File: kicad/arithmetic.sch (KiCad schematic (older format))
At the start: 73 parts, among them J1 Conn_01x03_Male, J2 Conn_01x05_Male, J3 Conn_01x05_Male, J4 Conn_Coaxial, J5 Conn_Coaxial, J6 Conn_Coaxial, U1 LM317, U2 LM337, U3 OPA197xD, U4 OPA197xD, U5 OPA197xD

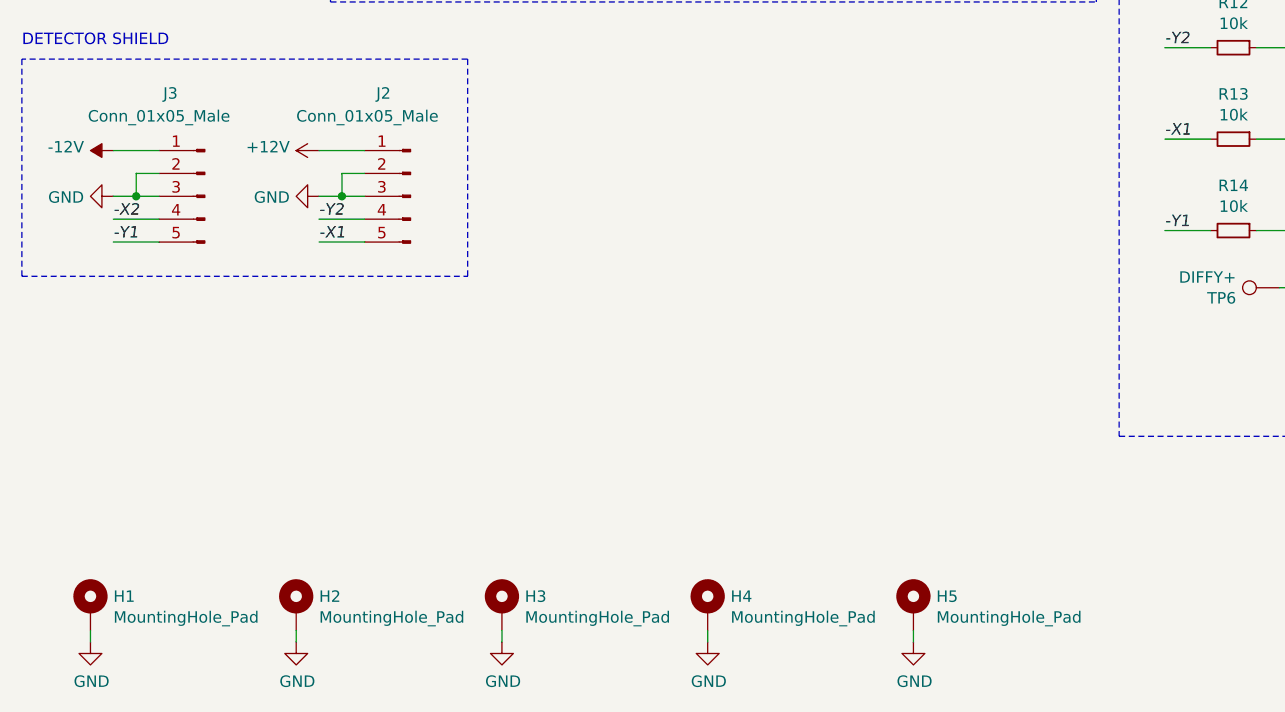
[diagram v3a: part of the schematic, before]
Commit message: adjusted arithmetic pcb for updated detector pcb
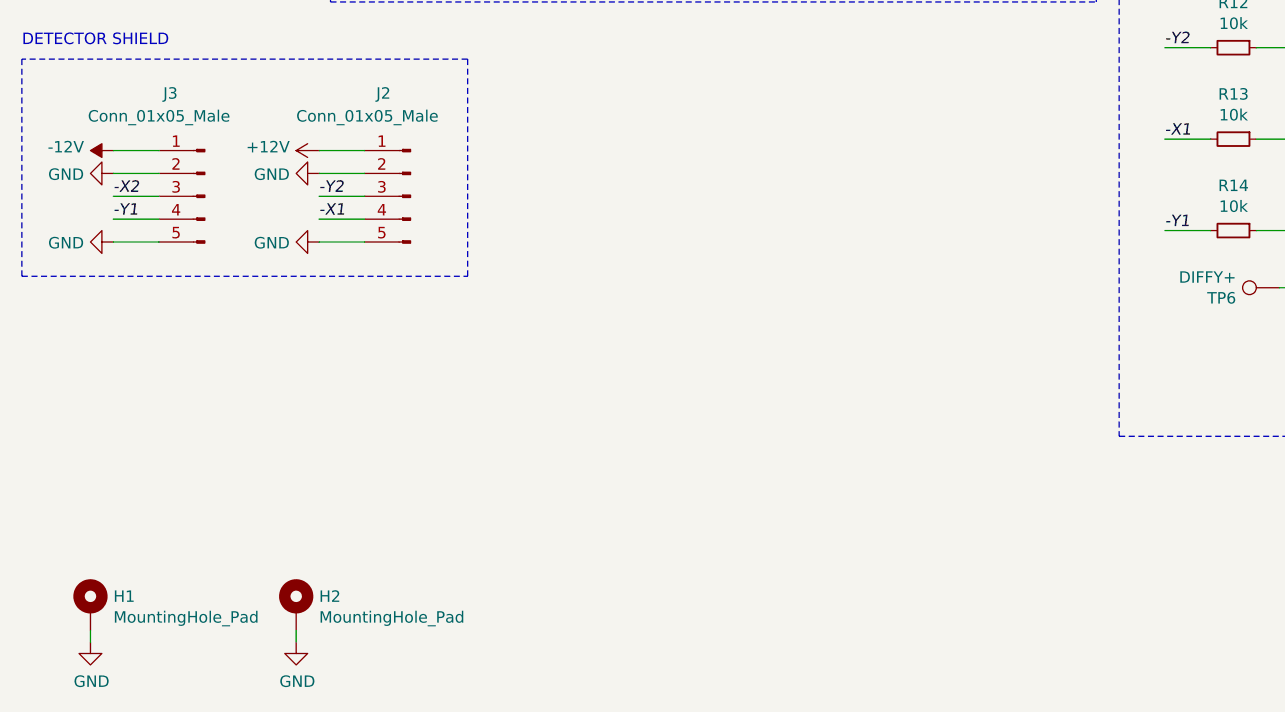
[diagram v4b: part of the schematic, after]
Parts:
- removed H3, H4, H5: MountingHole_Pad, MountingHole:MountingHole_2.7mm_M2.5_Pad, symbol Mechanical:MountingHole_Pad
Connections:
- net -X1: now also J2.4 (Pin_4); no longer J2.5 (Pin_5)
- net -X2: now also J3.3 (Pin_3); no longer J3.4 (Pin_4)
- net -Y1: now also J3.4 (Pin_4); no longer J3.5 (Pin_5)
- net -Y2: now also J2.3 (Pin_3); no longer J2.4 (Pin_4)
- net GND: now also J2.5 (Pin_5), J3.5 (Pin_5); no longer J2.3 (Pin_3), J3.3 (Pin_3)
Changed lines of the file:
@@
 Wire Notes Line
 	5300 750  1950 750
-Text Label 1900 5550 0    50   Italic 0
+Text Label 1900 5450 0    50   Italic 0
 -X1
+Text Label 1000 5350 0    50   Italic 0
+-X2
 Text Label 1000 5450 0    50   Italic 0
--X2
-Text Label 1000 5550 0    50   Italic 0
 -Y1
-Text Label 1900 5450 0    50   Italic 0
+Text Label 1900 5350 0    50   Italic 0
 -Y2
 Wire Wire Line
 	1000 5150 1200 5150
-Wire Wire Line
-	1200 5250 1100 5250
-Wire Wire Line
-	1000 5350 1100 5350
 Wire Wire Line
 	1200 5450 1000 5450
@@
 L power:GND #PWR02
 U 1 1 5EC11469
-P 1900 5350
+P 1900 5250
 AR Path="/5EC11469" Ref="#PWR02"  Part="1"
 AR Path="/5E48BEC6/5EC11469" Ref="#PWR?"  Part="1"
 AR Path="/5E4BE137/5EC11469" Ref="#PWR?"  Part="1"
-F 0 "#PWR02" H 1900 5100 50  0001 C CNN
-F 1 "GND" V 1905 5222 50  0000 R CNN
-F 2 "" H 1900 5350 50  0001 C CNN
-F 3 "" H 1900 5350 50  0001 C CNN
-	1    1900 5350
-	0    1    1    0
-$EndComp
-Wire Wire Line
-	2100 5250 2000 5250
-Wire Wire Line
-	2000 5250 2000 5350
-Wire Wire Line
-	2000 5350 1900 5350
-Wire Wire Line
-	2000 5350 2100 5350
-Connection ~ 2000 5350
+F 0 "#PWR02" H 1900 5000 50  0001 C CNN
+F 1 "GND" V 1905 5122 50  0000 R CNN
+F 2 "" H 1900 5250 50  0001 C CNN
+F 3 "" H 1900 5250 50  0001 C CNN
+	1    1900 5250
+	0    1    1    0
+$EndComp
 Wire Wire Line
 	2100 5450 1900 5450
@@
 	1800 7300 1800 7250
 $Comp
-L Mechanical:MountingHole_Pad H3
-U 1 1 5EAEAEF9
-P 2700 7150
-F 0 "H3" H 2800 7199 50  0000 L CNN
-F 1 "MountingHole_Pad" H 2800 7108 50  0000 L CNN
-F 2 "MountingHole:MountingHole_2.7mm_M2.5_Pad" H 2700 7150 50  0001 C CNN
-F 3 "~" H 2700 7150 50  0001 C CNN
-	1    2700 7150
-	1    0    0    -1
-$EndComp
-$Comp
-L power:GND #PWR0115
-U 1 1 5EAEAEFF
-P 2700 7300
-AR Path="/5EAEAEFF" Ref="#PWR0115"  Part="1"
-AR Path="/5E4BE137/5EAEAEFF" Ref="#PWR?"  Part="1"
-F 0 "#PWR0115" H 2700 7050 50  0001 C CNN
-F 1 "GND" H 2705 7127 50  0000 C CNN
-F 2 "" H 2700 7300 50  0001 C CNN
-F 3 "" H 2700 7300 50  0001 C CNN
-	1    2700 7300
-	1    0    0    -1
-$EndComp
-Wire Wire Line
-	2700 7300 2700 7250
-$Comp
-L Mechanical:MountingHole_Pad H4
-U 1 1 5EAF96D9
-P 3600 7150
-F 0 "H4" H 3700 7199 50  0000 L CNN
-F 1 "MountingHole_Pad" H 3700 7108 50  0000 L CNN
-F 2 "MountingHole:MountingHole_2.7mm_M2.5_Pad" H 3600 7150 50  0001 C CNN
-F 3 "~" H 3600 7150 50  0001 C CNN
-	1    3600 7150
-	1    0    0    -1
-$EndComp
-$Comp
-L power:GND #PWR0116
-U 1 1 5EAF96DF
-P 3600 7300
-AR Path="/5EAF96DF" Ref="#PWR0116"  Part="1"
-AR Path="/5E4BE137/5EAF96DF" Ref="#PWR?"  Part="1"
-F 0 "#PWR0116" H 3600 7050 50  0001 C CNN
-F 1 "GND" H 3605 7127 50  0000 C CNN
-F 2 "" H 3600 7300 50  0001 C CNN
-F 3 "" H 3600 7300 50  0001 C CNN
-	1    3600 7300
-	1    0    0    -1
-$EndComp
-Wire Wire Line
-	3600 7300 3600 7250
-$Comp
-L Mechanical:MountingHole_Pad H5
-U 1 1 5EB2DC32
-P 4500 7150
-F 0 "H5" H 4600 7199 50  0000 L CNN
-F 1 "MountingHole_Pad" H 4600 7108 50  0000 L CNN
-F 2 "MountingHole:MountingHole_2.7mm_M2.5_Pad" H 4500 7150 50  0001 C CNN
-F 3 "~" H 4500 7150 50  0001 C CNN
-	1    4500 7150
-	1    0    0    -1
-$EndComp
-$Comp
-L power:GND #PWR0117
-U 1 1 5EB2DC38
-P 4500 7300
-AR Path="/5EB2DC38" Ref="#PWR0117"  Part="1"
-AR Path="/5E4BE137/5EB2DC38" Ref="#PWR?"  Part="1"
-F 0 "#PWR0117" H 4500 7050 50  0001 C CNN
-F 1 "GND" H 4505 7127 50  0000 C CNN
-F 2 "" H 4500 7300 50  0001 C CNN
-F 3 "" H 4500 7300 50  0001 C CNN
-	1    4500 7300
-	1    0    0    -1
-$EndComp
-Wire Wire Line
-	4500 7300 4500 7250
-$Comp
 L power:GND #PWR0118
 U 1 1 5EB97CC8
-P 1000 5350
+P 1000 5250
 AR Path="/5EB97CC8" Ref="#PWR0118"  Part="1"
 AR Path="/5E48BEC6/5EB97CC8" Ref="#PWR?"  Part="1"
 AR Path="/5E4BE137/5EB97CC8" Ref="#PWR?"  Part="1"
-F 0 "#PWR0118" H 1000 5100 50  0001 C CNN
-F 1 "GND" V 1005 5222 50  0000 R CNN
-F 2 "" H 1000 5350 50  0001 C CNN
-F 3 "" H 1000 5350 50  0001 C CNN
-	1    1000 5350
-	0    1    1    0
-$EndComp
-Wire Wire Line
-	1100 5250 1100 5350
-Connection ~ 1100 5350
-Wire Wire Line
-	1100 5350 1200 5350
+F 0 "#PWR0118" H 1000 5000 50  0001 C CNN
+F 1 "GND" V 1005 5122 50  0000 R CNN
+F 2 "" H 1000 5250 50  0001 C CNN
+F 3 "" H 1000 5250 50  0001 C CNN
+	1    1000 5250
+	0    1    1    0
+$EndComp
 $Comp
 L power:+12V #PWR0119
@@
 Wire Notes Line
 	1800 2100 1800 3950
+Wire Wire Line
+	1000 5350 1200 5350
+Wire Wire Line
+	1000 5250 1200 5250
+$Comp
+L power:GND #PWR?
+U 1 1 5EB349D4
+P 1000 5550
+AR Path="/5EB349D4" Ref="#PWR?"  Part="1"
+AR Path="/5E48BEC6/5EB349D4" Ref="#PWR?"  Part="1"
+AR Path="/5E4BE137/5EB349D4" Ref="#PWR?"  Part="1"
+F 0 "#PWR?" H 1000 5300 50  0001 C CNN
+F 1 "GND" V 1005 5422 50  0000 R CNN
+F 2 "" H 1000 5550 50  0001 C CNN
+F 3 "" H 1000 5550 50  0001 C CNN
+	1    1000 5550
+	0    1    1    0
+$EndComp
+Wire Wire Line
+	1900 5350 2100 5350
+Wire Wire Line
+	1900 5250 2100 5250
+$Comp
+L power:GND #PWR?
+U 1 1 5EB438B6
+P 1900 5550
+AR Path="/5EB438B6" Ref="#PWR?"  Part="1"
+AR Path="/5E48BEC6/5EB438B6" Ref="#PWR?"  Part="1"
+AR Path="/5E4BE137/5EB438B6" Ref="#PWR?"  Part="1"
+F 0 "#PWR?" H 1900 5300 50  0001 C CNN
+F 1 "GND" V 1905 5422 50  0000 R CNN
+F 2 "" H 1900 5550 50  0001 C CNN
+F 3 "" H 1900 5550 50  0001 C CNN
+	1    1900 5550
+	0    1    1    0
+$EndComp
 $EndSCHEMATC

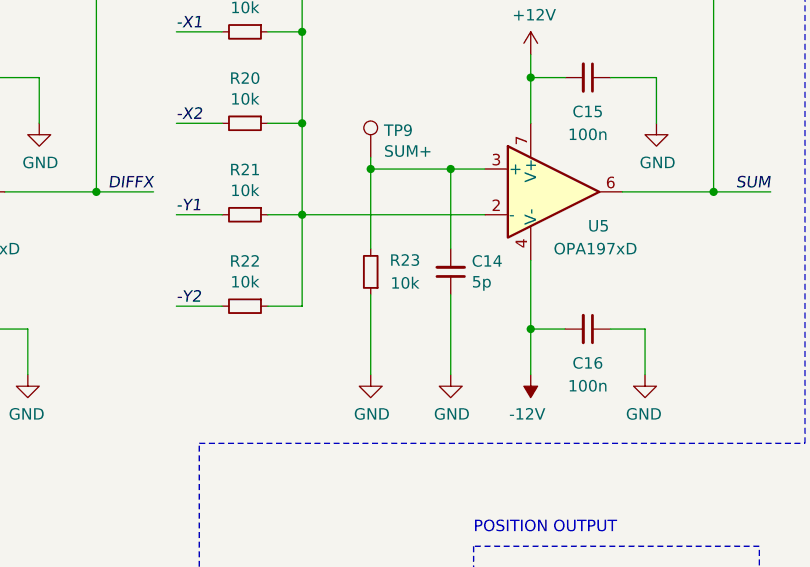
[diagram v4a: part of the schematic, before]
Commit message: applied suggestions from Bodo Hecker
* changed R23 to 2k
* replaced pin holes in detector with padded pin holes
* increased casing of led resistors to 1210
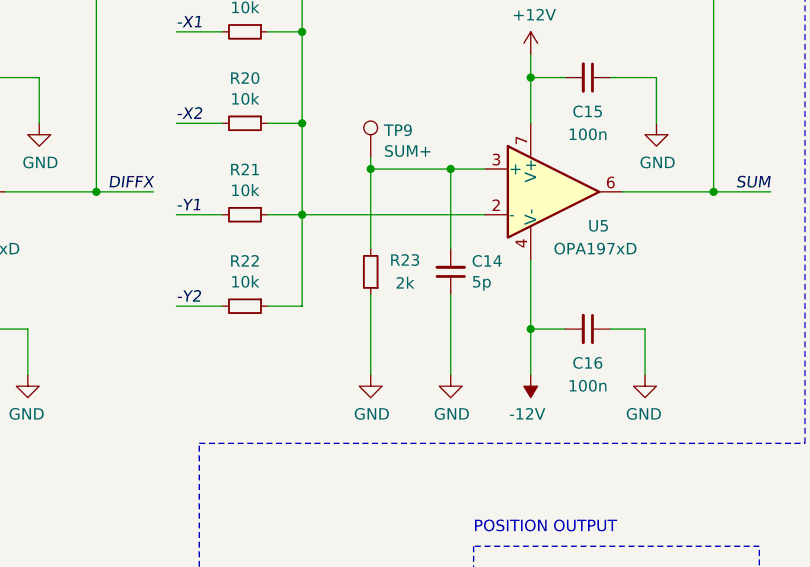
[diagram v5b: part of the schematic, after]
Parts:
- R11, R5: footprint Resistor_SMD:R_0603_1608Metric -> Resistor_SMD:R_1210_3225Metric
- R23: value 10k -> 2k
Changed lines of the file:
@@
 AR Path="/5E4BE137/5E92FC43" Ref="R?"  Part="1"
 F 0 "R23" H 9000 2750 50  0000 C CNN
-F 1 "10k" H 9000 2850 50  0000 C CNN
+F 1 "2k" H 9000 2850 50  0000 C CNN
 F 2 "Resistor_SMD:R_0603_1608Metric" H 9150 2800 50  0001 C CNN
 F 3 "~" H 9150 2800 50  0001 C CNN
@@
 $EndComp
 $Comp
-L power:+15V #PWR?
+L power:+15V #PWR0115
 U 1 1 5EA5D277
 P 1200 1450
-F 0 "#PWR?" H 1200 1300 50  0001 C CNN
+F 0 "#PWR0115" H 1200 1300 50  0001 C CNN
 F 1 "+15V" V 1215 1578 50  0000 L CNN
 F 2 "" H 1200 1450 50  0001 C CNN
@@
 $EndComp
 $Comp
-L power:GND #PWR?
+L power:GND #PWR0116
 U 1 1 5EA5D27D
 P 1200 1550
-F 0 "#PWR?" H 1200 1300 50  0001 C CNN
+F 0 "#PWR0116" H 1200 1300 50  0001 C CNN
 F 1 "GND" V 1200 1400 50  0000 R CNN
 F 2 "" H 1200 1550 50  0001 C CNN
@@
 $EndComp
 $Comp
-L power:-15V #PWR?
+L power:-15V #PWR0117
 U 1 1 5EA5D283
 P 1200 1650
-F 0 "#PWR?" H 1200 1750 50  0001 C CNN
+F 0 "#PWR0117" H 1200 1750 50  0001 C CNN
 F 1 "-15V" V 1215 1778 50  0000 L CNN
 F 2 "" H 1200 1650 50  0001 C CNN
@@
 $EndComp
 $Comp
-L power:PWR_FLAG #FLG?
+L power:PWR_FLAG #FLG0101
 U 1 1 5EA6B4AC
 P 1150 1450
-F 0 "#FLG?" H 1150 1525 50  0001 C CNN
+F 0 "#FLG0101" H 1150 1525 50  0001 C CNN
 F 1 "PWR_FLAG" V 1150 1577 50  0000 L CNN
 F 2 "" H 1150 1450 50  0001 C CNN
@@
 	1150 1450 1200 1450
 $Comp
-L power:PWR_FLAG #FLG?
+L power:PWR_FLAG #FLG0102
 U 1 1 5EA7A5FB
 P 1150 1550
-F 0 "#FLG?" H 1150 1625 50  0001 C CNN
+F 0 "#FLG0102" H 1150 1625 50  0001 C CNN
 F 1 "PWR_FLAG" V 1150 1677 50  0000 L CNN
 F 2 "" H 1150 1550 50  0001 C CNN
@@
 $EndComp
 $Comp
-L power:PWR_FLAG #FLG?
+L power:PWR_FLAG #FLG0103
 U 1 1 5EA7AA30
 P 1150 1650
-F 0 "#FLG?" H 1150 1725 50  0001 C CNN
+F 0 "#FLG0103" H 1150 1725 50  0001 C CNN
 F 1 "PWR_FLAG" V 1150 1777 50  0000 L CNN
 F 2 "" H 1150 1650 50  0001 C CNN
@@
 F 0 "R5" H 909 3096 50  0000 L CNN
 F 1 "510" H 909 3005 50  0000 L CNN
-F 2 "Resistor_SMD:R_0603_1608Metric" H 850 3050 50  0001 C CNN
+F 2 "Resistor_SMD:R_1210_3225Metric" H 850 3050 50  0001 C CNN
 F 3 "~" H 850 3050 50  0001 C CNN
 	1    850  3050
@@
 F 0 "R11" H 1459 3096 50  0000 L CNN
 F 1 "470" H 1459 3005 50  0000 L CNN
-F 2 "Resistor_SMD:R_0603_1608Metric" H 1400 3050 50  0001 C CNN
+F 2 "Resistor_SMD:R_1210_3225Metric" H 1400 3050 50  0001 C CNN
 F 3 "~" H 1400 3050 50  0001 C CNN
 	1    1400 3050
@@
 	1000 5250 1200 5250
 $Comp
-L power:GND #PWR?
+L power:GND #PWR0120
 U 1 1 5EB349D4
 P 1000 5550
-AR Path="/5EB349D4" Ref="#PWR?"  Part="1"
+AR Path="/5EB349D4" Ref="#PWR0120"  Part="1"
 AR Path="/5E48BEC6/5EB349D4" Ref="#PWR?"  Part="1"
 AR Path="/5E4BE137/5EB349D4" Ref="#PWR?"  Part="1"
-F 0 "#PWR?" H 1000 5300 50  0001 C CNN
+F 0 "#PWR0120" H 1000 5300 50  0001 C CNN
 F 1 "GND" V 1005 5422 50  0000 R CNN
 F 2 "" H 1000 5550 50  0001 C CNN
@@
 	1900 5250 2100 5250
 $Comp
-L power:GND #PWR?
+L power:GND #PWR0121
 U 1 1 5EB438B6
 P 1900 5550
-AR Path="/5EB438B6" Ref="#PWR?"  Part="1"
+AR Path="/5EB438B6" Ref="#PWR0121"  Part="1"
 AR Path="/5E48BEC6/5EB438B6" Ref="#PWR?"  Part="1"
 AR Path="/5E4BE137/5EB438B6" Ref="#PWR?"  Part="1"
-F 0 "#PWR?" H 1900 5300 50  0001 C CNN
+F 0 "#PWR0121" H 1900 5300 50  0001 C CNN
 F 1 "GND" V 1905 5422 50  0000 R CNN
 F 2 "" H 1900 5550 50  0001 C CNN

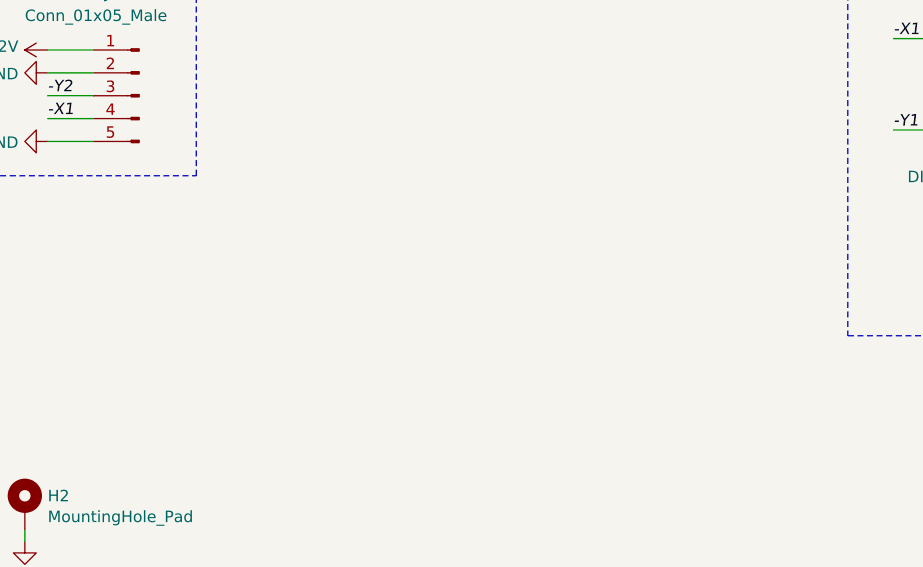
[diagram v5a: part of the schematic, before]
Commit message: updated file structure and latex sections
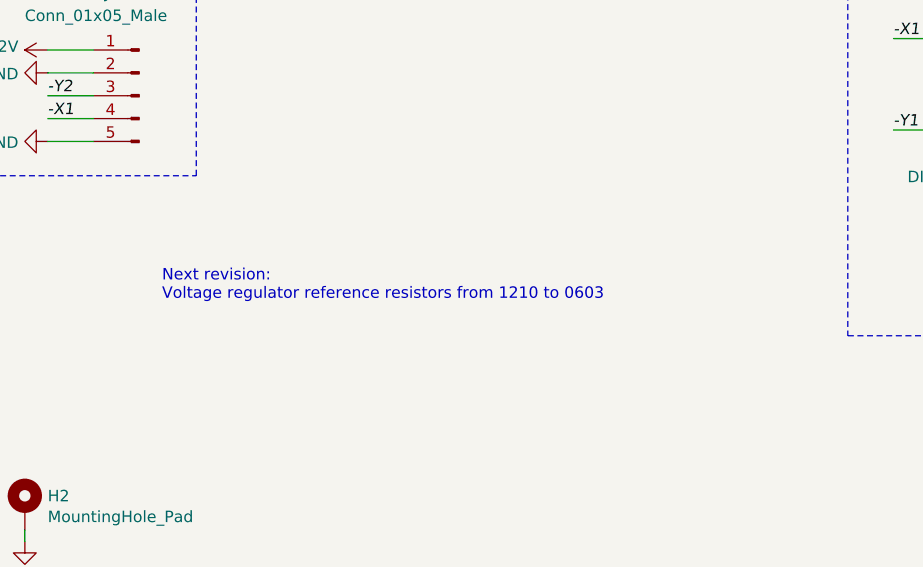
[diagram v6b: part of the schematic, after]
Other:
- note added: "Next revision:\nVoltage regulator reference resistors from 1210 to 0603"
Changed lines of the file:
@@
 	0    1    1    0
 $EndComp
+Text Notes 2400 6250 0    50   ~ 0
+Next revision:\nVoltage regulator reference resistors from 1210 to 0603
 $EndSCHEMATC

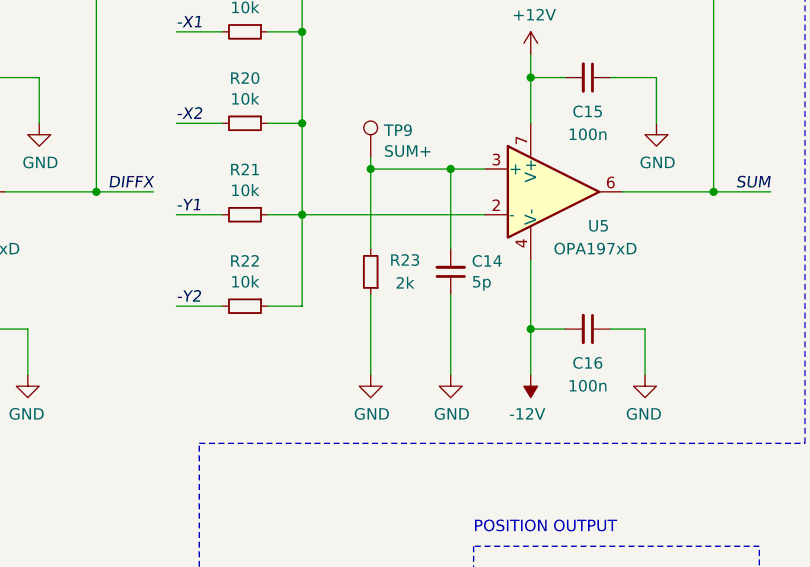
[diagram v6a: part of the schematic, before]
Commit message: added arithmetic amplifier circuit to schematic section
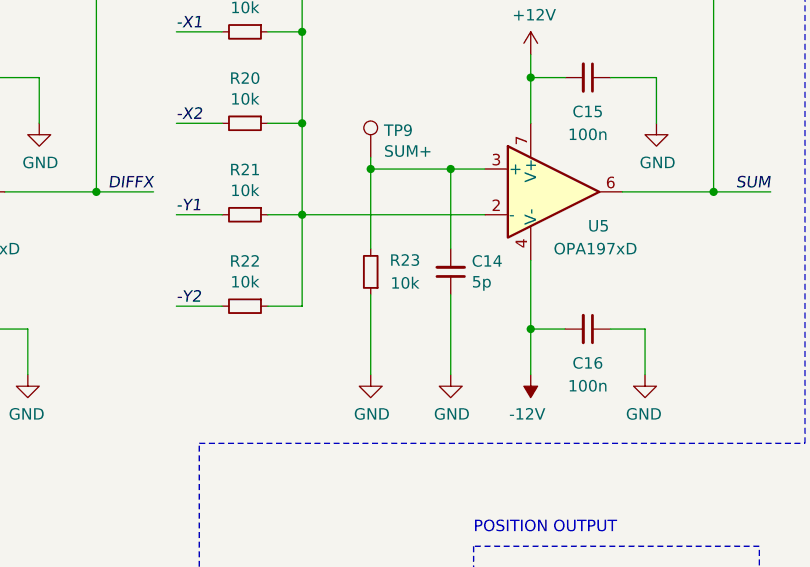
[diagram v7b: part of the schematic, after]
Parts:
- R23: value 2k -> 10k
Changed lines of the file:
@@
 AR Path="/5E4BE137/5E92FC43" Ref="R?"  Part="1"
 F 0 "R23" H 9000 2750 50  0000 C CNN
-F 1 "2k" H 9000 2850 50  0000 C CNN
+F 1 "10k" H 9000 2850 50  0000 C CNN
 F 2 "Resistor_SMD:R_0603_1608Metric" H 9150 2800 50  0001 C CNN
 F 3 "~" H 9150 2800 50  0001 C CNN
